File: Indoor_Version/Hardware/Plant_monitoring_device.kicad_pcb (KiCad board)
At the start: 2 copper layers, 79 x 79 mm, 62 parts, among them J1 Barrel_Jack, J10 A2501WR-2P1, J11 A2501WR-3P1, J12 A2501WR-3P1, J13 A2501WR-3P1, J14 A2501WR-3P1, J2 Header_1x6, J3 A2501WR-2P1, J4 A2501WR-2P1, J5 A2501WR-2P1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

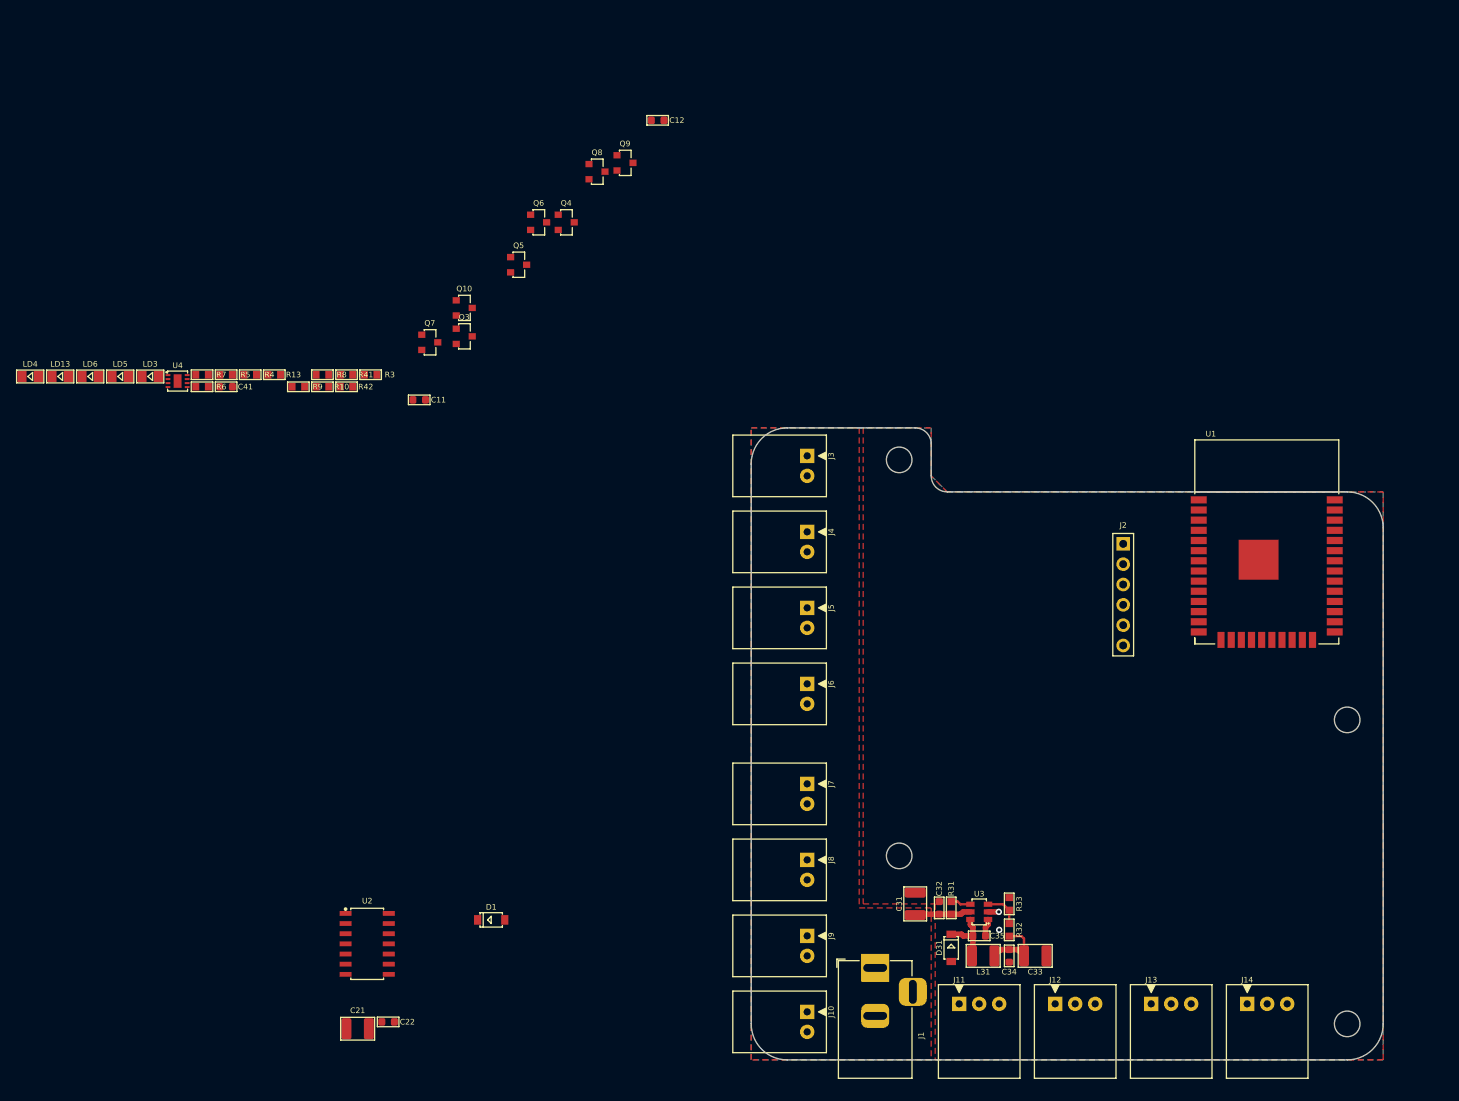
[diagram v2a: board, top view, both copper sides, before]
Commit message: Finished design of the indoor version of the gardener. Generated gerbers.
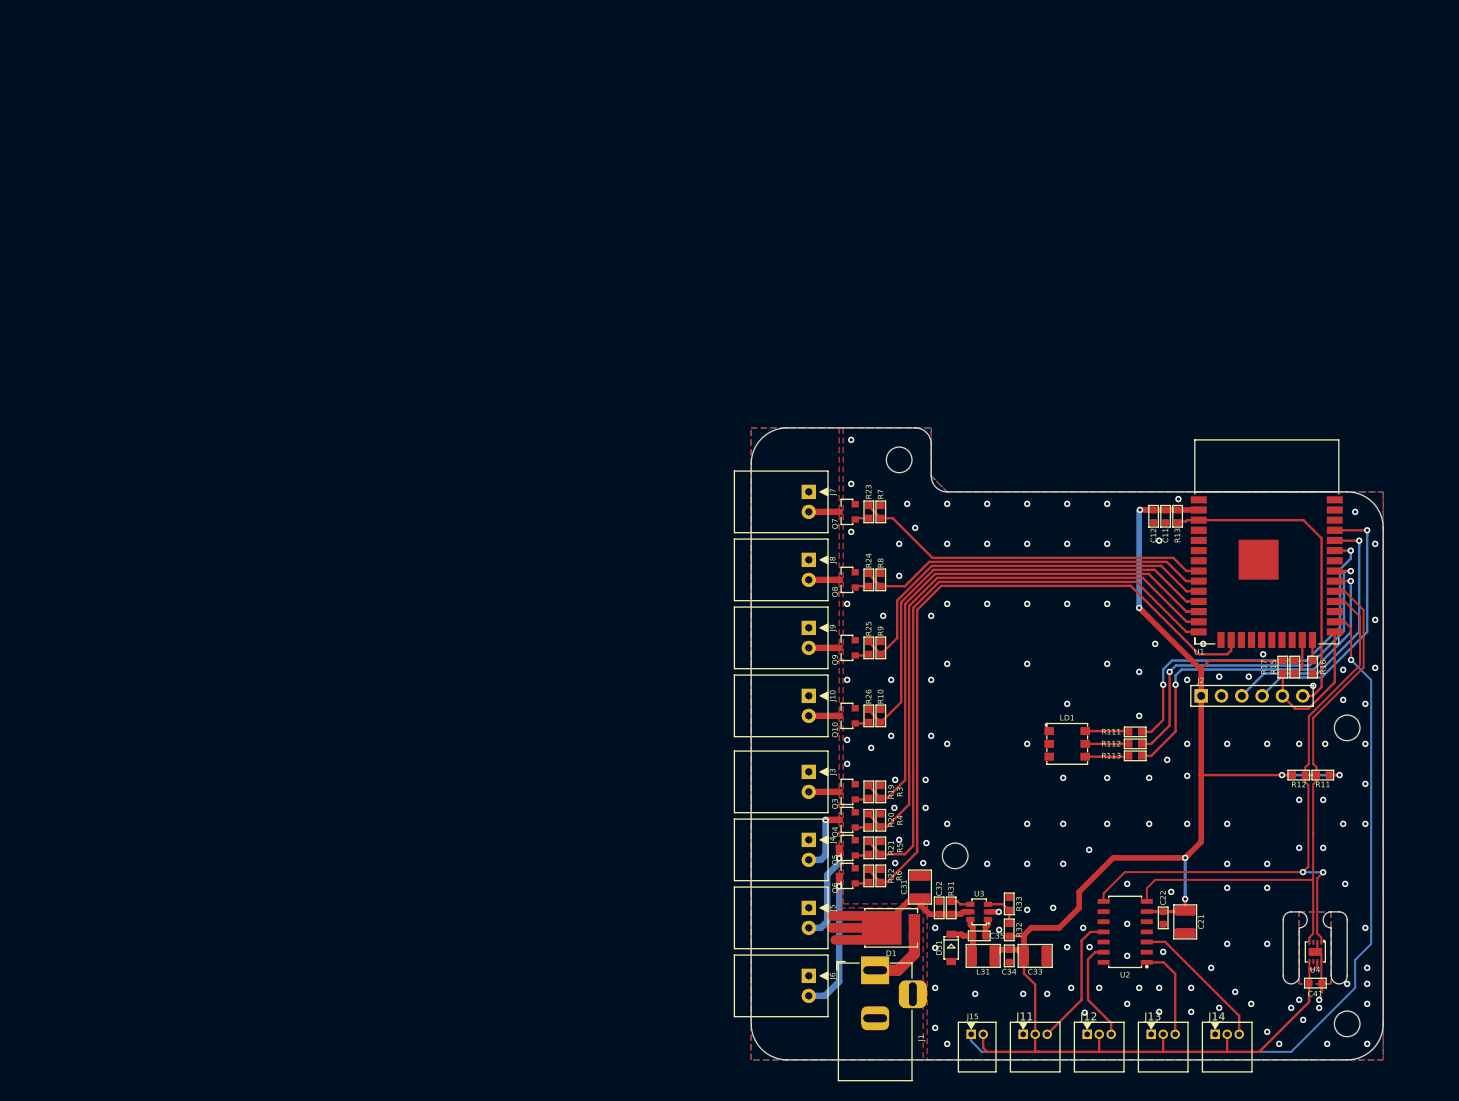
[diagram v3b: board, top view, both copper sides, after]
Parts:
- removed LD13: RED, MRS_Diodes:LED_0805
- removed LD3, LD4, LD5, LD6: ORANGE, MRS_Diodes:LED_0805
- removed R41, R42: 10k, MRS_Passives:R0603
- added H111: Mr_Gardener_Logo_Small, Logos:mrg_gardener_12mm, B.Cu at (244.5, 90.5)
- added J15: S2B-ZR, MRS_Connectors:S2B-ZR, F.Cu at (208.0, 146.3)
- added LD1: RF-W2SA50TS-A39R, MRS_Diodes:RF-W2SA50TS-A39R, F.Cu at (220.0, 110.0)
- added R11: 10k, MRS_Passives:R0603, F.Cu at (251.9, 113.9)
- added R111: 150R, MRS_Passives:R0603, F.Cu at (228.5, 108.5)
- added R112: 150R, MRS_Passives:R0603, F.Cu at (228.5, 110.0)
- added R113: 150R, MRS_Passives:R0603, F.Cu at (228.5, 111.5)
- added R12: 10k, MRS_Passives:R0603, F.Cu at (248.9, 113.9)
- added R15: 10k, MRS_Passives:R0603, F.Cu at (248.4, 100.4)
- added R16: 10k, MRS_Passives:R0603, F.Cu at (250.7, 100.4)
- added R17: 10k, MRS_Passives:R0603, F.Cu at (246.9, 100.4)
- added R19: 1k, MRS_Passives:R0603, F.Cu at (195.2, 116.0)
- added R20: 1k, MRS_Passives:R0603, F.Cu at (195.2, 119.5)
- added R21: 1k, MRS_Passives:R0603, F.Cu at (195.2, 123.0)
- added R22: 1k, MRS_Passives:R0603, F.Cu at (195.2, 126.5)
- added R23: 1k, MRS_Passives:R0603, F.Cu at (195.2, 81.0)
- added R24: 1k, MRS_Passives:R0603, F.Cu at (195.2, 89.5)
- added R25: 1k, MRS_Passives:R0603, F.Cu at (195.2, 98.0)
- added R26: 1k, MRS_Passives:R0603, F.Cu at (195.2, 106.5)
- D1: value MBR230LSFT1G -> PPS1045-3G; footprint MRS_Diodes:SOD-123 -> MRS_TO:TO-277-3
- J11, J12, J13, J14: value A2501WR-3P1 -> S3B-ZR; footprint MRS_Connectors:A2501WR-3P1 -> MRS_Connectors:S3B-ZR
- R13, R3, R4, R5, R6: value 1k -> 10k
- moved U4 159.1 mm to (251.0, 136.0), turned to 270 degrees
- moved C41 155.2 mm to (251.0, 139.9)
- moved R13 114.3 mm to (233.8, 81.5), turned to 270 degrees
- moved R6 104.6 mm to (196.7, 126.5), turned to 90 degrees
- moved C21 104.3 mm to (234.8, 132.2), turned to 270 degrees
- moved R5 101.0 mm to (196.7, 123.0), turned to 90 degrees
- moved C22 97.8 mm to (232.0, 131.8), turned to 270 degrees
- moved R4 96.5 mm to (196.7, 119.5), turned to 90 degrees
- moved U2 94.8 mm to (227.2, 133.5), turned to 180 degrees
- moved C11 94.4 mm to (232.3, 81.5), turned to 270 degrees
- moved Q6 90.3 mm to (192.5, 126.5), turned to 180 degrees
- moved R7 86.6 mm to (196.7, 81.0), turned to 90 degrees
- moved Q5 83.7 mm to (192.5, 123.0), turned to 180 degrees
- moved Q4 82.5 mm to (192.5, 119.5), turned to 180 degrees
- moved R3 82.4 mm to (196.7, 116.0), turned to 90 degrees
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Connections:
- J11 pad 1: +3V3 -> GND
- J11 pad 2: /ADC_SOIL1 -> +3V3
- J11 pad 3: GND -> /ADC_SOIL1
- J12 pad 1: +3V3 -> GND
- J12 pad 2: /ADC_SOIL2 -> +3V3
- J12 pad 3: GND -> /ADC_SOIL2
- J13 pad 1: +3V3 -> GND
- J13 pad 2: /ADC_SOIL3 -> +3V3
- J13 pad 3: GND -> /ADC_SOIL3
- J14 pad 1: +3V3 -> GND
- J14 pad 2: /ADC_SOIL4 -> +3V3
- J14 pad 3: GND -> /ADC_SOIL4
- Q10 pad 1: /LED_PWM4 -> Net-(Q10-Pad1)
- Q3 pad 1: /OUT1 -> Net-(Q3-Pad1)
- Q4 pad 1: /OUT2 -> Net-(Q4-Pad1)
- Q5 pad 1: /OUT3 -> Net-(Q5-Pad1)
- Q6 pad 1: /OUT4 -> Net-(Q6-Pad1)
- Q7 pad 1: /LED_PWM1 -> Net-(Q7-Pad1)
- Q8 pad 1: /LED_PWM2 -> Net-(Q8-Pad1)
- Q9 pad 1: /LED_PWM3 -> Net-(Q9-Pad1)
- R13 pad 1: /SIG_PWM -> +3V3
- R13 pad 2: Net-(LD13-Pad2) -> /EN
- R3 pad 1: /OUT1 -> /PUMP1
- R3 pad 2: Net-(LD3-Pad2) -> GND
- R4 pad 1: /OUT2 -> /PUMP2
- R4 pad 2: Net-(LD4-Pad2) -> GND
- R5 pad 1: /OUT3 -> /PUMP3
- R5 pad 2: Net-(LD5-Pad2) -> GND
- R6 pad 1: /OUT4 -> /PUMP4
- R6 pad 2: Net-(LD6-Pad2) -> GND
- U1 pad 10: Net-(U1-Pad10) -> /LED_PWM3
- U1 pad 11: Net-(U1-Pad11) -> /LED_PWM4
- U1 pad 12: Net-(U1-Pad12) -> /PUMP1
- U1 pad 13: Net-(U1-Pad13) -> /PUMP2
- U1 pad 14: Net-(U1-Pad14) -> /PUMP3
- U1 pad 15: Net-(U1-Pad15) -> GND
- U1 pad 16: Net-(U1-Pad16) -> /PUMP4
- U1 pad 26: Net-(U1-Pad26) -> /WATER_LVL_SW
- U1 pad 28: Net-(U1-Pad28) -> /I2C_SDA
- U1 pad 29: Net-(U1-Pad29) -> /I2C_SCL
- U1 pad 30: Net-(U1-Pad30) -> /PWM_LED_B
- U1 pad 31: Net-(U1-Pad31) -> /PWM_LED_R
- U1 pad 33: Net-(U1-Pad33) -> /PWM_LED_G
- U1 pad 8: Net-(U1-Pad8) -> /LED_PWM1
- U1 pad 9: Net-(U1-Pad9) -> /LED_PWM2
- U2 pad 1: /ADC_SOIL1 -> /ADC_SOIL3
- U2 pad 11: /ADC_SOIL3 -> /ADC_SOIL1
- U2 pad 13: /ADC_SOIL4 -> /ADC_SOIL2
- U2 pad 3: /ADC_SOIL2 -> /ADC_SOIL4
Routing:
- net +3V3: track 8.62 -> 204.6 mm, vias 0 -> 6
- net /WATER_LVL_SW: track 0.00 -> 101.9 mm, vias 0 -> 1
- net /PUMP4: track 0.00 -> 84.1 mm
- net /I2C_SDA: track 0.00 -> 78.0 mm, vias 0 -> 2
- net /PUMP3: track 0.00 -> 76.1 mm
- net /I2C_SCL: track 0.00 -> 72.6 mm
- net /PUMP2: track 0.00 -> 71.6 mm
- net /PUMP1: track 0.00 -> 68.4 mm
- net /LED_PWM4: track 0.00 -> 58.8 mm
- net /LED_PWM3: track 0.00 -> 50.6 mm
- net /PWM_LED_G: track 0.00 -> 46.0 mm, vias 0 -> 2
- net /PWM_LED_R: track 0.00 -> 45.3 mm, vias 0 -> 2
- net /PWM_LED_B: track 0.00 -> 45.1 mm, vias 0 -> 2
- net /LED_PWM1: track 0.00 -> 44.6 mm
- net /LED_PWM2: track 0.00 -> 44.2 mm
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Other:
- outline, holes or cut-outs redrawn
- board text added: "Mr. Gardener"
- board text added: "SIDE HOLES FOR AIR"
- board text added: "rev 1"
